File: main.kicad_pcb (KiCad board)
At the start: 4 copper layers, 65 x 56 mm, 122 parts, among them J1 RPi UART Debug LEDs, J10 Debug connector, J11 Debug connector, J12 Debug connector, J13 Debug connector, J16 Debug connector, J17 Debug connector, J2 mini iso blue, J3 LCD power, J4 VAN Debug LEDs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

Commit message: 2 layer PCB
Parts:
- removed C1: 1uF, Capacitor_SMD:C_0805_2012Metric
- removed C6: 0.1uF, Capacitor_SMD:C_0805_2012Metric
- removed D10, D15, D16, D19, D2, D3, D5, D6, D7, D8, D9: LED, LED_SMD:LED_0402_1005Metric
- removed the G*** at (135.7, 92.5)
- removed J1: RPi UART Debug LEDs, Connector_PinHeader_2.54mm:PinHeader_1x03_P2.54mm_Vertical
- removed J10, J11: Debug connector, TestPoint:TestPoint_Loop_D1.80mm_Drill1.0mm_Beaded
- removed J12, J13: Debug connector, TestPoint:TestPoint_Keystone_5000-5004_Miniature
- removed J16 (x2), J17, J6, J8, J9: Debug connector, TestPoint:TestPoint_Pad_D1.0mm
- removed J4: VAN Debug LEDs, Connector_PinHeader_2.54mm:PinHeader_1x03_P2.54mm_Vertical
- removed J5: UART LED Debug Switch, Connector_PinHeader_2.54mm:PinHeader_1x03_P2.54mm_Vertical
- removed Q5, Q6: NMOS, Package_TO_SOT_SMD:SOT-723
- removed R10, R11, R16, R9: 3200, Resistor_SMD:R_0805_2012Metric
- removed R110, R118: 100K, Resistor_SMD:R_0201_0603Metric
- removed R14, R15: 1k, Resistor_SMD:R_0805_2012Metric
- removed R17, R4: 10.2k, Resistor_SMD:R_0805_2012Metric
- removed R18: 1.5k, Resistor_SMD:R_0805_2012Metric
- removed R21: 10k, Resistor_SMD:R_0603_1608Metric_Pad0.98x0.95mm_HandSolder
- removed R5, R8: 3.2k, Resistor_SMD:R_0805_2012Metric
- added TP1: TestPoint, TestPoint:TestPoint_Pad_D1.0mm, F.Cu at (112.0, 118.2)
- added TP2: TestPoint, TestPoint:TestPoint_Pad_D1.0mm, F.Cu at (113.7, 99.4)
- added TP3: TestPoint, TestPoint:TestPoint_Pad_D1.0mm, F.Cu at (165.2, 101.4)
- added TP4: TestPoint, TestPoint:TestPoint_Pad_D1.0mm, F.Cu at (142.4, 100.6)
- added TP5: TestPoint, TestPoint:TestPoint_Pad_D1.0mm, F.Cu at (161.5, 108.0)
- added TP6: TestPoint, TestPoint:TestPoint_Pad_D1.0mm, F.Cu at (112.0, 121.8)
- added TP7: TestPoint, TestPoint:TestPoint_Pad_D1.0mm, F.Cu at (112.0, 125.0)
- added TP8: TestPoint, TestPoint:TestPoint_Pad_D1.0mm, F.Cu at (122.9, 124.3)
- added TP9: TestPoint, TestPoint:TestPoint_Pad_D1.0mm, F.Cu at (120.2, 118.1)
- R1: value 10k -> 4k7; footprint Resistor_SMD:R_0603_1608Metric_Pad0.98x0.95mm_HandSolder -> Resistor_SMD:R_0603_1608Metric
- R2: value 1M -> 2M
- R3: value 200k -> 523k
- U6: footprint RF_Module:ESP32-WROOM-32D -> intoftainment:esp32_altered
- moved C208 48.5 mm to (149.0, 91.9)
- moved R109 48.5 mm to (149.8, 91.2)
- moved C200 48.5 mm to (152.9, 95.1)
- moved C202 48.5 mm to (146.8, 95.5)
- moved C204 48.5 mm to (149.7, 99.6)
- moved C205 48.5 mm to (157.3, 99.6)
- moved C209 48.5 mm to (151.9, 92.4)
- moved C82 48.5 mm to (155.3, 99.6)
- moved C83 48.5 mm to (153.3, 99.6)
- moved D1 48.5 mm to (147.9, 91.7)
- moved D4 48.5 mm to (146.2, 98.5)
- moved L12 48.5 mm to (156.9, 95.3)
- moved R107 48.5 mm to (152.9, 93.6)
- moved R108 48.5 mm to (147.7, 93.3)
- moved R111 48.5 mm to (150.6, 91.5)
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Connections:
- net /ECU_comms/TSS_MISO renamed TSS_MISO
- net /ECU_comms/TSS_MOSI renamed TSS_MOSI
- net /ECU_comms/TSS_SS renamed TSS_SS
- net /ESP32-WROOM/RX renamed RX
- net /ESP32-WROOM/TX renamed TX
- MP8759GD1 pad 6: Net-(MP8759GD1-MODE) -> unconnected-(MP8759GD1-MODE-Pad6)
- MP8759GD3 pad 6: Net-(MP8759GD3-MODE) -> unconnected-(MP8759GD3-MODE-Pad6)
- R1 pad 1: Net-(Q6-S) -> Net-(U4-Rs)
- U10 pad 3: ESP_TSS_SCK -> TSS Interrupt 3.3V
- U10 pad 9: /ECU_comms/TSS_SCLK -> TSS Interrupt 5V
- U11 pad 11: +5V Ignition -> +5V Car Battery
- U11 pad 4: TSS Interrupt 3.3V -> ESP_TSS_SCK
- U11 pad 8: TSS Interrupt 5V -> TSS_CLK
- U3 pad 14: /ECU_comms/TSS Reset -> unconnected-(U3-RESET-Pad14)
- U3 pad 15: /ECU_comms/TSS_SCLK -> TSS_CLK
- U4 pad 8: /ECU_comms/RS -> Net-(U4-Rs)
- U6 pad 30: ESP_TSS_Reset -> ESP_TSS_OE
- U6 pad 37: ESP_MCP_RS -> unconnected-(U6-IO23-Pad37)
- U6 pad 8: ESP_TSS_OE -> unconnected-(U6-IO32-Pad8)
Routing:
- net +5V Car Battery: track 22.5 -> 121.7 mm
- net +12V Ignition: track 71.8 -> 0.00 mm, vias 2 -> 0
- net VAN_RX: track 82.3 -> 21.9 mm, vias 1 -> 2
- net TX: track 66.5 -> 10.4 mm, vias 2 -> 0
- net RX: track 63.7 -> 12.7 mm, vias 2 -> 0
- net VAN_TX: track 67.5 -> 20.9 mm, vias 1 -> 0
- net RPi_TX: track 76.8 -> 36.7 mm, vias 1 -> 2
- net RPi_RX: track 70.1 -> 30.1 mm, vias 1 -> 2
- net +3V3 Car Battery: track 47.9 -> 87.2 mm, vias 3 -> 6
- net +5V Ignition: track 17.2 -> 49.2 mm, vias 13 -> 0
- net ESP_TSS_OE: track 42.8 -> 16.0 mm, vias 2 -> 0
- net +12V Car Battery: track 76.6 -> 53.1 mm, vias 2 -> 6
- net ESP_TSS_Reset: track 22.6 -> 0.00 mm
- net ESP_MCP_RS: track 19.7 -> 0.00 mm
- net EN: track 51.4 -> 34.1 mm, vias 3 -> 2
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- removed copper zone on In2.Cu, net +3V3 Car Battery
- removed copper zone on In2.Cu, net +5V Car Battery
- removed copper zone on In1.Cu, net +5V Ignition
- removed copper zone on F.Cu, net ESP_ADC1_CH5
- removed copper zone on In2.Cu, net Net-(P1-Pin_1)
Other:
- outline, holes or cut-outs redrawn
- copper layers 4 -> 2
- board text added: "R1"
- board text removed: "12V Battery"
- board text removed: "12V Ignition"
- board text removed: "3.3V Battery"
- board text removed: "5V Battery"
- board text removed: "5V Ignition"
- board text removed: "BOOT"
- board text removed: "Debug LEDs"
- board text removed: "ESP Flash"
- board text removed: "Power LEDs"
- board text removed: "RPi UART"
- board text removed: "RX"
- board text removed: "TX"
- board text removed: "VAN"

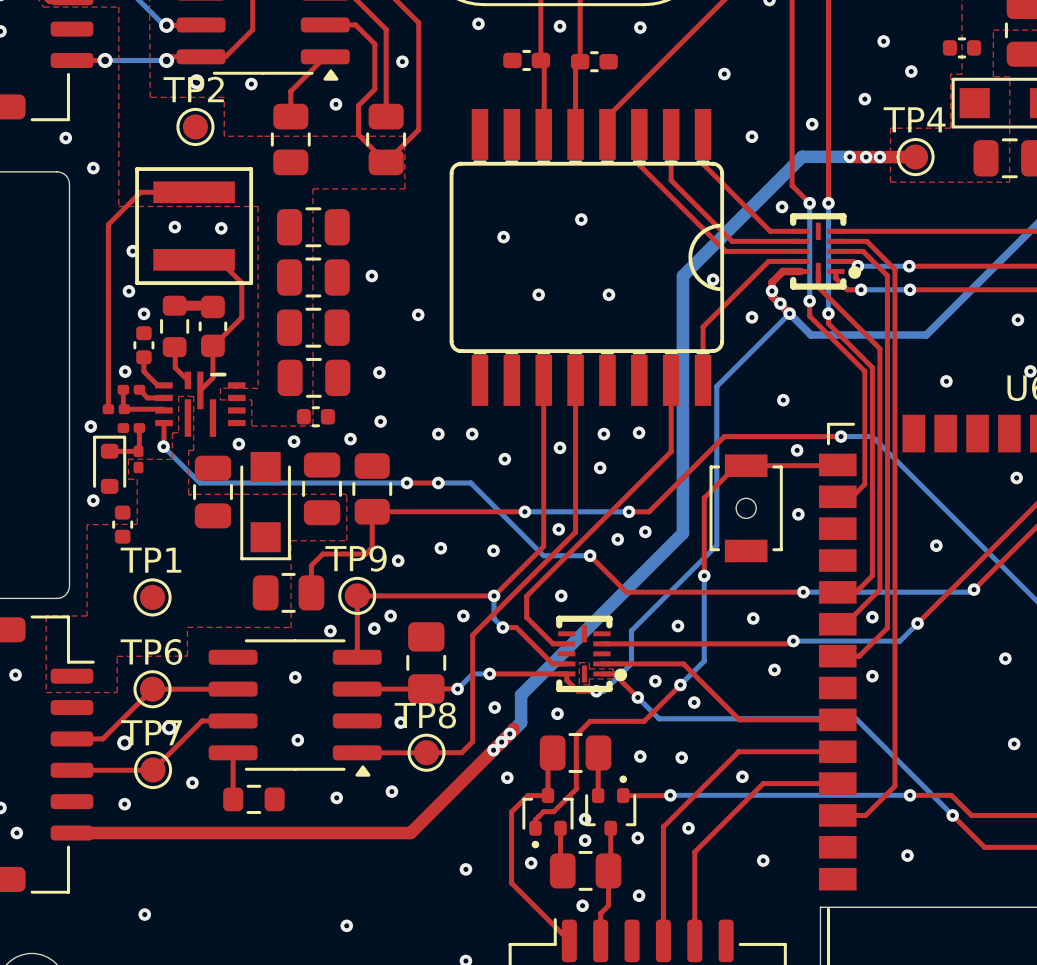
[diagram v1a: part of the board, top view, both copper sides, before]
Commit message: changed the CAN transceiever; fixed the transiever typo
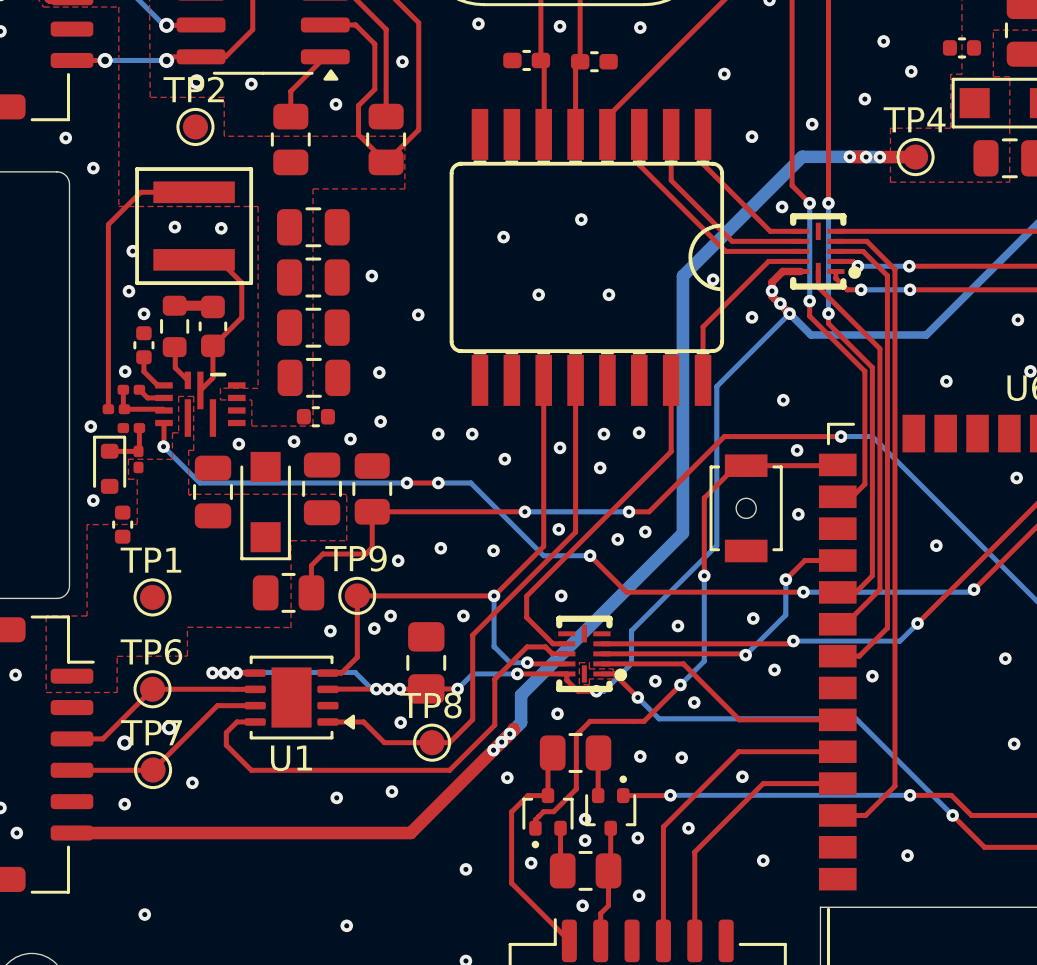
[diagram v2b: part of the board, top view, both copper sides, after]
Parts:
- removed R1: 4k7, Resistor_SMD:R_0603_1608Metric
- removed U4: MCP2551-I-SN, Package_SO:SOIC-8_3.9x4.9mm_P1.27mm
- added U1: TJA1051TK-3, Package_SON:HVSON-8-1EP_3x3mm_P0.65mm_EP1.6x2.4mm, F.Cu at (117.5, 122.1)
- moved TP8 0.46 mm to (123.1, 123.9)
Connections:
- net /ECU_comms/XTAL1 renamed XTAL1
- net /ECU_comms/XTAL2 renamed XTAL2
- U11 pad 3: unconnected-(U11-A2-Pad3) -> ESP_TJA_S
- U11 pad 9: unconnected-(U11-B2-Pad9) -> TJA_S
- U6 pad 28: unconnected-(U6-IO17-Pad28) -> ESP_TJA_S
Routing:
- net TJA_S: track 0.00 -> 19.0 mm
- net ESP_TJA_S: track 0.00 -> 11.8 mm, vias 0 -> 2
- net +5V Car Battery: track 121.7 -> 132.4 mm, vias 14 -> 20
- net VAN_RX: track 21.9 -> 23.9 mm
- net Net-(U4-Rs): track 1.86 -> 0.00 mm
- net VAN_H: track 7.24 -> 8.37 mm
- net VAN_L: track 7.24 -> 8.12 mm
- net VAN_TX: track 20.9 -> 21.6 mm
- net +12V Car Battery: track 53.1 -> 53.8 mm
- net GND: vias 166 -> 162

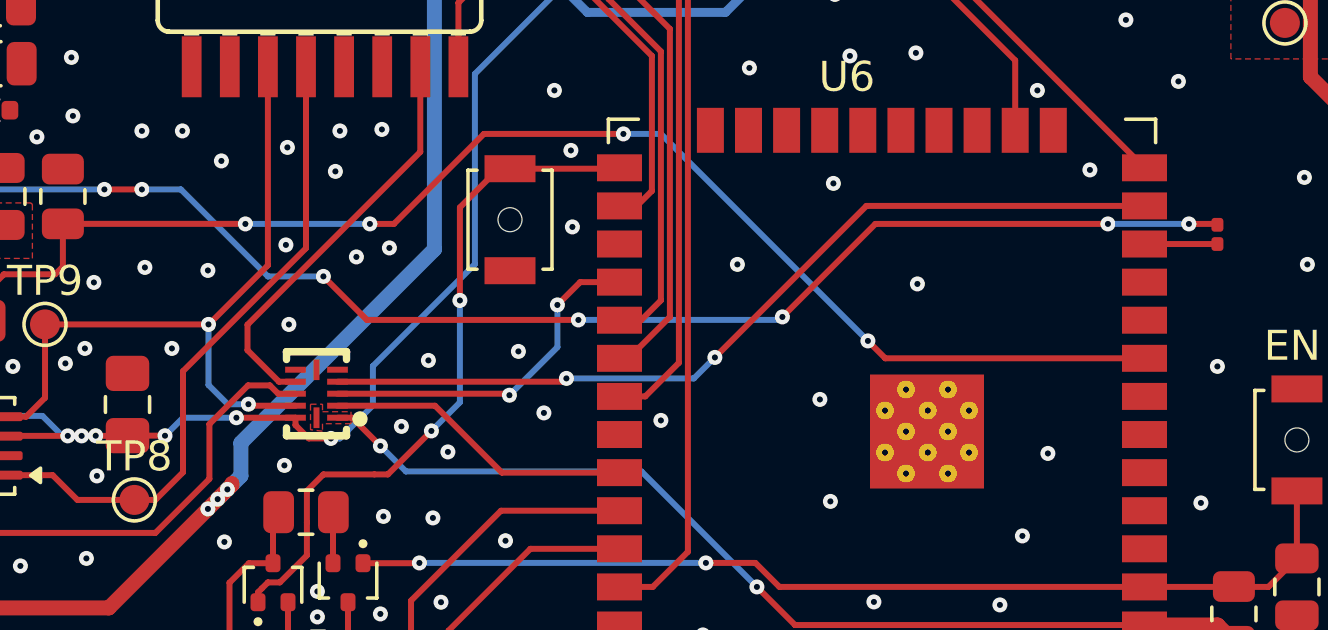
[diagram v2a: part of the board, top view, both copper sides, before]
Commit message: added direct VAN_TX to ESP connection
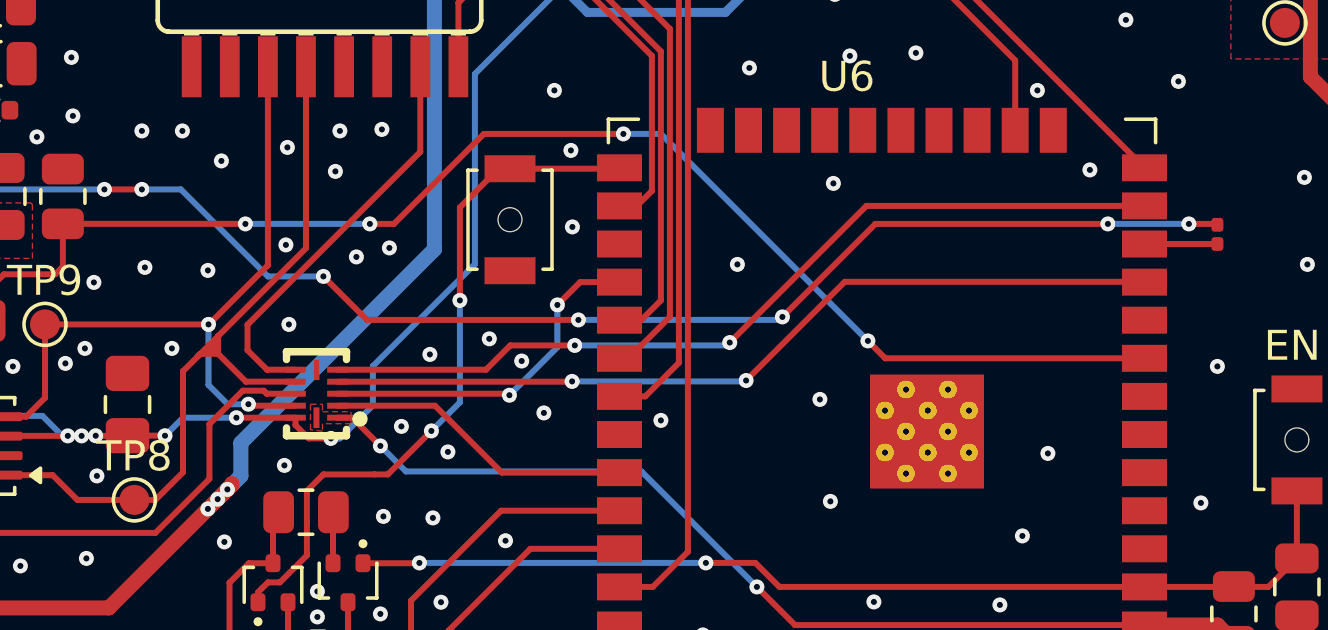
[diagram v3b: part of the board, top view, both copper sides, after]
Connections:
- U11 pad 4: ESP_TSS_SCK -> VAN_TX_3V3
- U11 pad 5: unconnected-(U11-A4-Pad5) -> ESP_TSS_SCK
- U11 pad 7: unconnected-(U11-B4-Pad7) -> TSS_CLK
- U11 pad 8: TSS_CLK -> VAN_TX
- U6 pad 11: unconnected-(U6-IO26-Pad11) -> VAN_TX_3V3
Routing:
- net VAN_TX_3V3: track 0.00 -> 28.3 mm, vias 0 -> 2
- net VAN_TX: track 21.6 -> 26.7 mm

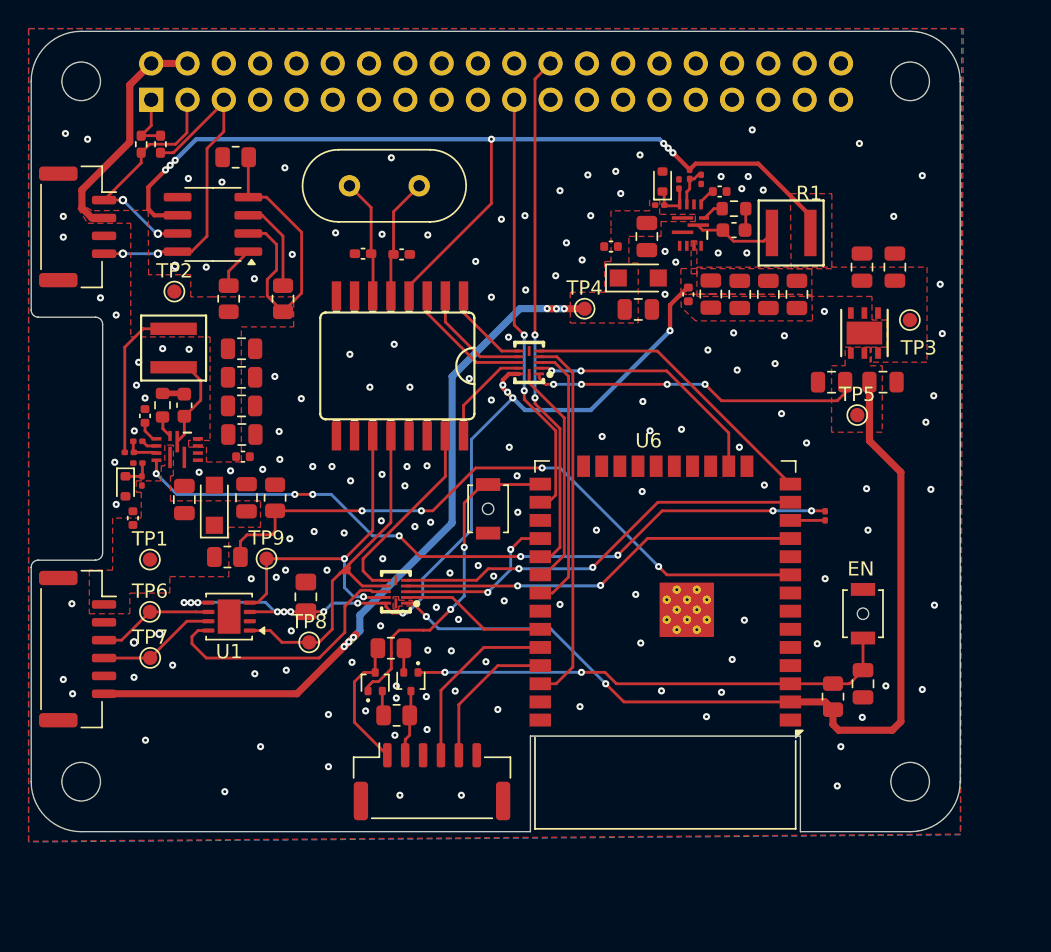
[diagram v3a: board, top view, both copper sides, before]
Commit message: changed power regulators, updated PCB
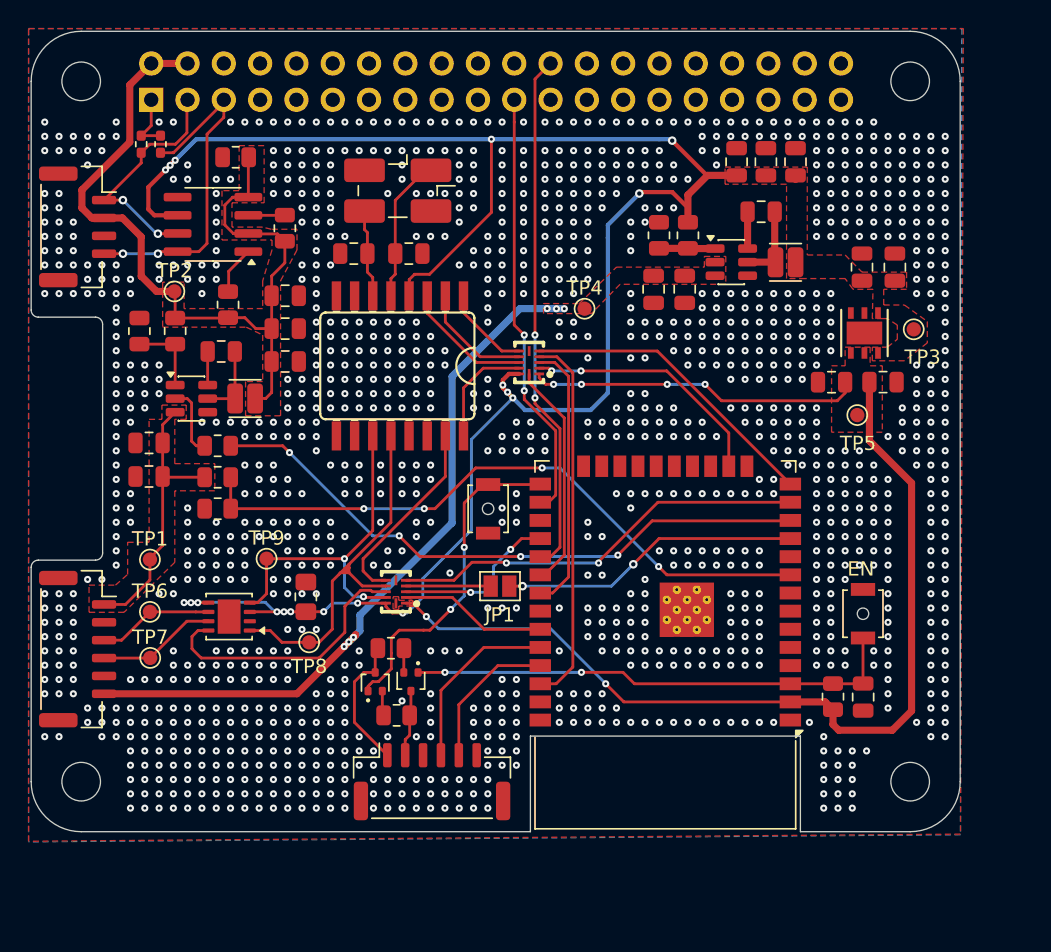
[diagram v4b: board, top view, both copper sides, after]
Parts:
- removed C200, C222: 220nF, Capacitor_SMD:C_0603_1608Metric
- removed C202, C205, C206, C216, C219, C220, C81, C82, C83, C87, C88, C89: 22uF, Capacitor_SMD:C_0805_2012Metric
- removed C203, C204, C217, C218: 100nF, Capacitor_SMD:C_0402_1005Metric
- removed C208, C221: 220nF, Capacitor_SMD:C_0201_0603Metric
- removed C209, C223: 1uF, Capacitor_SMD:C_0402_1005Metric
- removed D1, D18: BZX585-B3V3,135, Diode_SMD:D_SOD-523
- removed D17, D4: VTVS25ASMF-M3-08, Diode_SMD:Nexperia_CFP3_SOD-123W
- removed L12, L14: 1.5uH, intoftainment:IND_XGL4030_COC
- removed MP8759GD1, MP8759GD3: C200, intoftainment:QFN-12_MP8759_MNP
- removed R107, R120: 3.3, Resistor_SMD:R_0603_1608Metric
- removed R108, R117: 10k, Resistor_SMD:R_0201_0603Metric
- removed R109, R121: 41.2k, Resistor_SMD:R_0201_0603Metric
- removed R111, R119: 5.6k, Resistor_SMD:R_0201_0603Metric
- removed Y2: 8MHz, Crystal:Crystal_HC49-4H_Vertical
- added C1: 100nF, Capacitor_SMD:C_0805_2012Metric, F.Cu at (147.2, 99.2)
- added C14: 22uF, Capacitor_SMD:C_0805_2012Metric, F.Cu at (155.1, 90.3)
- added C15: 22uF, Capacitor_SMD:C_0805_2012Metric, F.Cu at (157.2, 90.3)
- added C16: 10uF, Capacitor_SMD:C_0805_2012Metric, F.Cu at (111.9, 110.0)
- added C17: 100nF, Capacitor_SMD:C_0805_2012Metric, F.Cu at (111.9, 112.3)
- added C18: 100nF, Capacitor_SMD:C_0805_2012Metric, F.Cu at (117.0, 103.6)
- added C19: 22uF, Capacitor_SMD:C_0805_2012Metric, F.Cu at (121.5, 104.3)
- added C20: 22uF, Capacitor_SMD:C_0805_2012Metric, F.Cu at (121.5, 102.0)
- added C21: 22uF, Capacitor_SMD:C_0805_2012Metric, F.Cu at (121.5, 99.7)
- added C4: 10uF, Capacitor_SMD:C_0805_2012Metric, F.Cu at (149.4, 99.2)
- added C5: 100nF, Capacitor_SMD:C_0805_2012Metric, F.Cu at (154.8, 93.8)
- added C6: 22uF, Capacitor_SMD:C_0805_2012Metric, F.Cu at (153.0, 90.3)
- added JP1: SolderJumper_2_Open, Jumper:SolderJumper-2_P1.3mm_Open_Pad1.0x1.5mm, F.Cu at (136.5, 120.0)
- added L1: VLS201612HBX-6R8M-1, Inductor_SMD:L_Cenker_CKCS201610, F.Cu at (156.5, 97.3)
- added L2: VLS201612HBX-6R8M-1, Inductor_SMD:L_Cenker_CKCS201610, F.Cu at (118.7, 106.9)
- added R1: 158k, Resistor_SMD:R_0805_2012Metric, F.Cu at (149.6, 95.5)
- added R4: 30.1k, Resistor_SMD:R_0805_2012Metric, F.Cu at (147.6, 95.5)
- added R5: 158k, Resistor_SMD:R_0805_2012Metric, F.Cu at (113.8, 102.2)
- added R8: 30.1k, Resistor_SMD:R_0805_2012Metric, F.Cu at (111.3, 102.2)
- added U4: AP63301WU-7, Package_TO_SOT_SMD:TSOT-23-6, F.Cu at (152.7, 97.3)
- added U5: AP63301WU-7, Package_TO_SOT_SMD:TSOT-23-6, F.Cu at (114.9, 106.9)
- added U8: ABM3B-8.000MHZ-B2-T, Crystal:Crystal_SMD_EuroQuartz_MJ-4Pin_5.0x3.2mm_HandSoldering, F.Cu at (129.3, 92.3)
- C7, C8: footprint Capacitor_SMD:C_0402_1005Metric_Pad0.74x0.62mm_HandSolder -> Capacitor_SMD:C_0805_2012Metric
- R122: footprint Resistor_SMD:R_0201_0603Metric -> Resistor_SMD:R_0805_2012Metric
- moved R122 42.8 mm to (116.7, 110.2), turned to 0 degrees
- moved R2 5.62 mm to (116.7, 112.4)
- moved R7 4.94 mm to (121.4, 95.0)
- moved R3 4.09 mm to (116.7, 114.6), turned to 180 degrees
- moved C2 0.93 mm to (161.9, 127.8)
- moved TP3 0.70 mm to (165.4, 102.0)
- moved C8 0.65 mm to (126.3, 96.7)
- moved C7 0.51 mm to (130.1, 96.7)
- moved R6 0.42 mm to (117.5, 100.3)
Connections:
- R122 pad 1: 5V_Ignition_Regulator_EN -> Net-(U5-EN)
- R122 pad 2: Net-(MP8759GD3-EN) -> 5V_Ignition_Regulator_EN
- U6 pad 11: VAN_TX_3V3 -> Net-(JP1-A)
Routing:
- net Net-(MP8759GD3-EN): track 51.5 -> 0.00 mm, vias 8 -> 0
- net 5V_Ignition_Regulator_EN: track 2.43 -> 43.4 mm, vias 0 -> 4
- net VAN_TX_3V3: track 28.3 -> 5.93 mm, vias 2 -> 0
- net Net-(JP1-A): track 0.00 -> 21.1 mm, vias 0 -> 2
- net +12V Ignition: track 0.00 -> 19.3 mm
- net +5V Ignition: track 49.2 -> 57.2 mm
- net Net-(MP8759GD3-SW): track 7.25 -> 0.00 mm
- net +5V Car Battery: track 132.4 -> 139.4 mm, vias 20 -> 18
- net Net-(MP8759GD1-SW): track 5.80 -> 0.00 mm
- net Net-(U4-SW): track 0.00 -> 5.44 mm
- net Net-(U5-FB): track 0.00 -> 5.36 mm
- net Net-(U5-SW): track 0.00 -> 5.22 mm
- net Net-(U5-EN): track 0.00 -> 5.00 mm
- net Net-(U4-FB): track 0.00 -> 3.93 mm
- net Net-(U7-~{INT}/SQW): track 6.50 -> 2.58 mm
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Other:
- board text removed: "R1"
